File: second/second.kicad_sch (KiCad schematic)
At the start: 5 parts

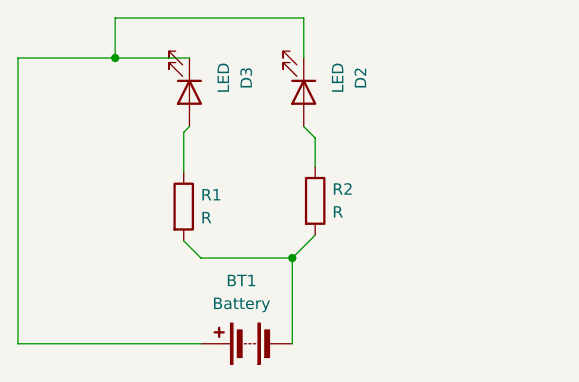
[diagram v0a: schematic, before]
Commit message: adding some no connects
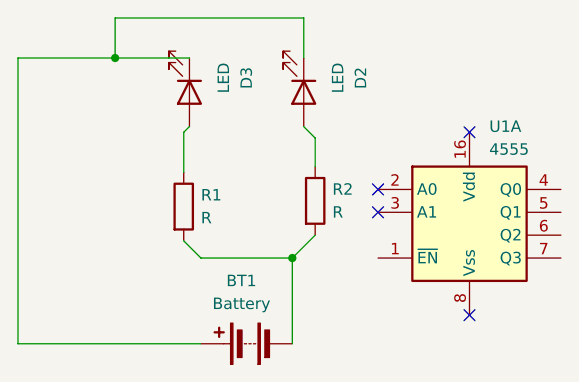
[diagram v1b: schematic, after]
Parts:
- added U1: 4555, symbol 4xxx_IEEE:4555
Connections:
- no-connect marks 0 -> 4
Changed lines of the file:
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@@
   (junction (at 121.92 88.265) (diameter 0) (color 0 0 0 0)
   )
+  (no_connect (at 141.605 74.295))
+  (no_connect (at 131.445 80.645))
+  (no_connect (at 141.605 94.615))
+  (no_connect (at 131.445 83.185))
   (wire (pts (xy 124.46 78.105) (xy 124.46 74.93))
     (stroke (width 0) (type default))
@@
         )
       )
+    )
+  )
+  (symbol (lib_id "4xxx_IEEE:4555") (at 141.605 84.455 0) (unit 1)
+    (in_bom yes) (on_board yes) (dnp no) (fields_autoplaced)
+    (property "Reference" "U1" (at 143.7991 73.66 0)
+      (effects (font (size 1.27 1.27)) (justify left))
+    )
+    (property "Value" "4555" (at 143.7991 76.2 0)
+      (effects (font (size 1.27 1.27)) (justify left))
+    )
+    (property "Footprint" "" (at 141.605 84.455 0)
+      (effects (font (size 1.27 1.27)) hide)
+    )
+    (property "Datasheet" "" (at 141.605 84.455 0)
+      (effects (font (size 1.27 1.27)) hide)
+    )
+    (pin "1")
+    (pin "13")
+    (pin "2")
+    (pin "5")
+    (pin "3")
+    (pin "16")
+    (pin "8")
+    (pin "14")
+    (pin "9")
+    (pin "4")
+    (pin "15")
+    (pin "12")
+    (pin "11")
+    (pin "10")
+    (pin "7")
+    (pin "6")
+    (instances
+      (project "second"
+        (path "/78df1c42-d07c-48d3-8d04-e695be2c9903"
+          (reference "U1") (unit 1)
+        )
+      )
